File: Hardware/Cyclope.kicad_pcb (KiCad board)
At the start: 2 copper layers, 30 x 100 mm, 75 parts, among them J1 M20-9762042, J2 Motor_2, J3 Motor_1, J4 Front, J5 Front, J8 FTDI, M1 FS5113R, M2 FS5113R, Q1 DMG3414U, Q2 DMG2301L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

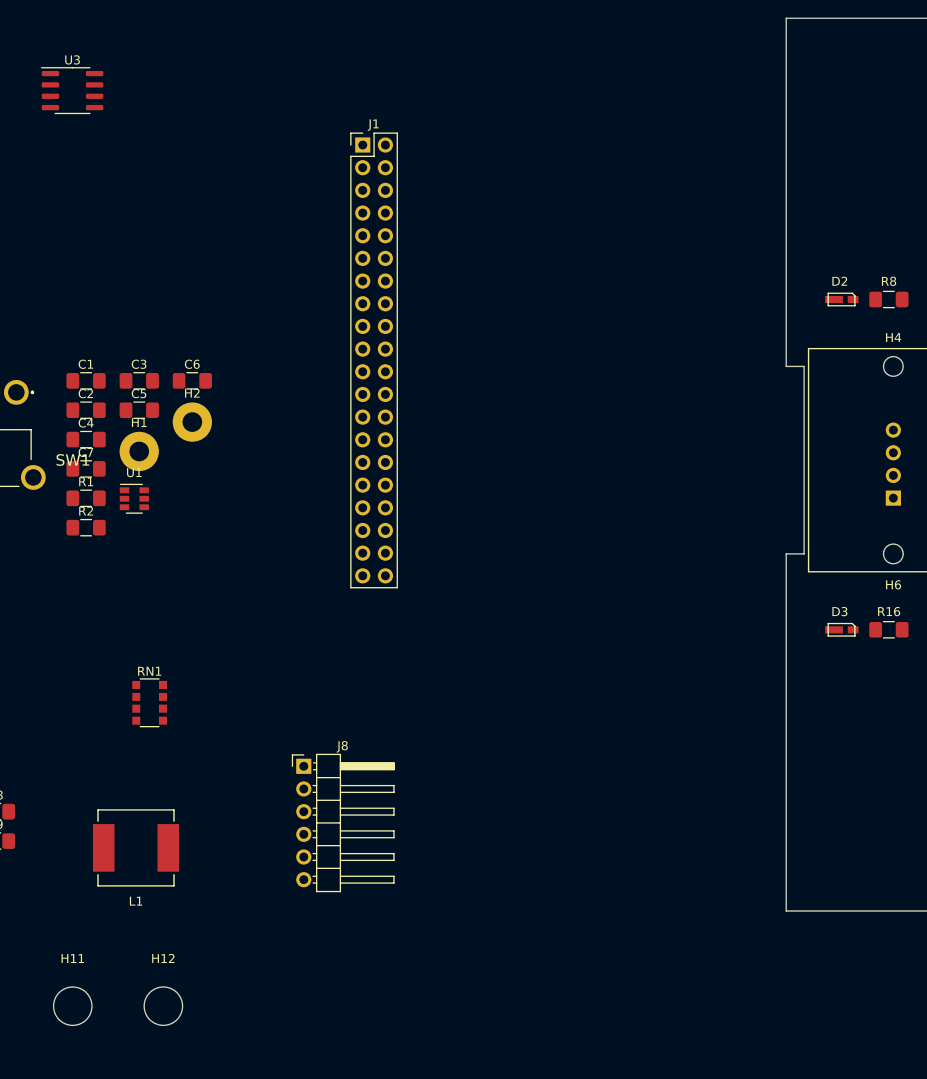
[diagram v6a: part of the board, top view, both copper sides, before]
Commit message: [Hardware] Changed front board mounting holes footprint to match angle bracket holes and positionned holes on front board PCB.
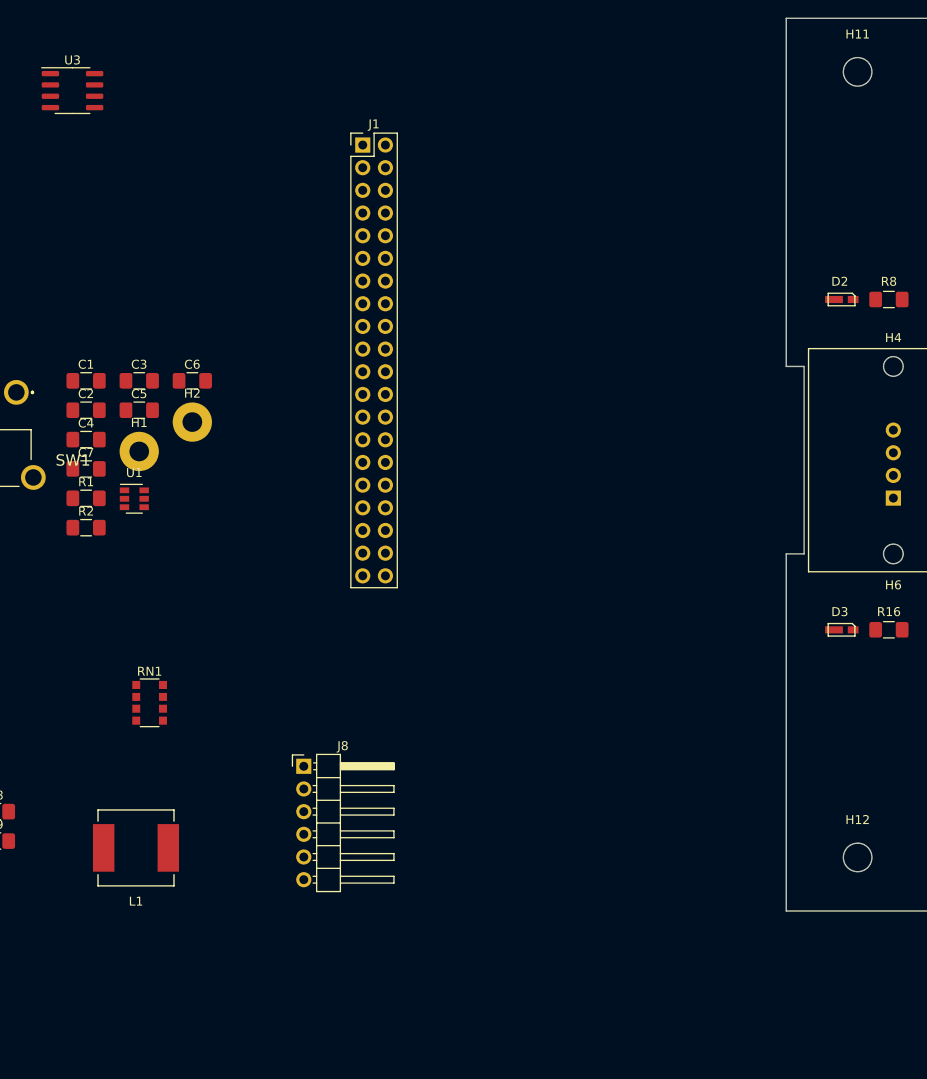
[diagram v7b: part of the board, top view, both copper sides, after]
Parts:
- H11, H12: footprint MountingHole:MountingHole_4.3mm_M4 -> MountingHole:MountingHole_3.2mm_M3
- moved H11 136.7 mm to (218.0, 36.0)
- moved H12 79.5 mm to (218.0, 124.0)
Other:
- board text added: "Use 8mm instead of 10mm to get some margin."
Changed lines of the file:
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@@
   (general
     (thickness 1.6)
-    (drawings 22)
+    (drawings 27)
     (tracks 0)
     (zones 0)
@@
     (add_net "Net-(SW1-Pad1)")
   )
+  (module MountingHole:MountingHole_3.2mm_M3 (layer F.Cu)
+    (at 218 124)
+    (descr "Mounting Hole 3.2mm, no annular, M3")
+    (tags "mounting hole 3.2mm no annular m3")
+    (attr virtual)
+    (fp_text reference H12 (at 0 -4.2) (layer F.SilkS)
+      (effects (font (size 1 1) (thickness 0.15)))
+    )
+    (fp_text value Front_Board (at 0 4.2) (layer F.Fab)
+      (effects (font (size 1 1) (thickness 0.15)))
+    )
+    (fp_circle (center 0 0) (end 3.45 0) (layer F.CrtYd) (width 0.05))
+    (fp_circle (center 0 0) (end 3.2 0) (layer Cmts.User) (width 0.15))
+    (fp_text user %R (at 0.3 0) (layer F.Fab)
+      (effects (font (size 1 1) (thickness 0.15)))
+    )
+    (pad 1 np_thru_hole circle (at 0 0) (size 3.2 3.2) (drill 3.2) (layers *.Cu *.Mask))
+  )
+  (module MountingHole:MountingHole_3.2mm_M3 (layer F.Cu)
+    (at 218 36)
+    (descr "Mounting Hole 3.2mm, no annular, M3")
+    (tags "mounting hole 3.2mm no annular m3")
+    (attr virtual)
+    (fp_text reference H11 (at 0 -4.2) (layer F.SilkS)
+      (effects (font (size 1 1) (thickness 0.15)))
+    )
+    (fp_text value Front_Board (at 0 4.2) (layer F.Fab)
+      (effects (font (size 1 1) (thickness 0.15)))
+    )
+    (fp_circle (center 0 0) (end 3.45 0) (layer F.CrtYd) (width 0.05))
+    (fp_circle (center 0 0) (end 3.2 0) (layer Cmts.User) (width 0.15))
+    (fp_text user %R (at 0.3 0) (layer F.Fab)
+      (effects (font (size 1 1) (thickness 0.15)))
+    )
+    (pad 1 np_thru_hole circle (at 0 0) (size 3.2 3.2) (drill 3.2) (layers *.Cu *.Mask))
+  )
   (module Resistor_SMD:R_1206_3216Metric_Pad1.42x1.75mm_HandSolder (layer F.Cu)
     (at 228.5 98.5)
@@
       (rotate (xyz 0 0 0))
     )
-  )
-  (module MountingHole:MountingHole_4.3mm_M4 (layer F.Cu)
-    (at 140.225001 140.665)
-    (descr "Mounting Hole 4.3mm, no annular, M4")
-    (tags "mounting hole 4.3mm no annular m4")
-    (attr virtual)
-    (fp_text reference H12 (at 0 -5.3) (layer F.SilkS)
-      (effects (font (size 1 1) (thickness 0.15)))
-    )
-    (fp_text value Front_Board (at 0 5.3) (layer F.Fab) hide
-      (effects (font (size 1 1) (thickness 0.15)))
-    )
-    (fp_circle (center 0 0) (end 4.55 0) (layer F.CrtYd) (width 0.05))
-    (fp_circle (center 0 0) (end 4.3 0) (layer Cmts.User) (width 0.15))
-    (fp_text user %R (at 0.3 0) (layer F.Fab)
-      (effects (font (size 1 1) (thickness 0.15)))
-    )
-    (pad 1 np_thru_hole circle (at 0 0) (size 4.3 4.3) (drill 4.3) (layers *.Cu *.Mask))
-  )
-  (module MountingHole:MountingHole_4.3mm_M4 (layer F.Cu)
-    (at 130.075001 140.665)
-    (descr "Mounting Hole 4.3mm, no annular, M4")
-    (tags "mounting hole 4.3mm no annular m4")
-    (attr virtual)
-    (fp_text reference H11 (at 0 -5.3) (layer F.SilkS)
-      (effects (font (size 1 1) (thickness 0.15)))
-    )
-    (fp_text value Front_Board (at 0 5.3) (layer F.Fab) hide
-      (effects (font (size 1 1) (thickness 0.15)))
-    )
-    (fp_circle (center 0 0) (end 4.55 0) (layer F.CrtYd) (width 0.05))
-    (fp_circle (center 0 0) (end 4.3 0) (layer Cmts.User) (width 0.15))
-    (fp_text user %R (at 0.3 0) (layer F.Fab)
-      (effects (font (size 1 1) (thickness 0.15)))
-    )
-    (pad 1 np_thru_hole circle (at 0 0) (size 4.3 4.3) (drill 4.3) (layers *.Cu *.Mask))
   )
   (module 158301250:158301250 (layer F.Cu)
@@
     )
   )
+  (dimension 8 (width 0.15) (layer Dwgs.User)
+    (gr_text "8,000 mm" (at 214 134.3) (layer Dwgs.User)
+      (effects (font (size 1 1) (thickness 0.15)))
+    )
+    (feature1 (pts (xy 218 130) (xy 218 133.586421)))
+    (feature2 (pts (xy 210 130) (xy 210 133.586421)))
+    (crossbar (pts (xy 210 133) (xy 218 133)))
+    (arrow1a (pts (xy 218 133) (xy 216.873496 133.586421)))
+    (arrow1b (pts (xy 218 133) (xy 216.873496 132.413579)))
+    (arrow2a (pts (xy 210 133) (xy 211.126504 133.586421)))
+    (arrow2b (pts (xy 210 133) (xy 211.126504 132.413579)))
+  )
+  (dimension 12 (width 0.15) (layer Dwgs.User)
+    (gr_text "12,000 mm" (at 205.7 124 90) (layer Dwgs.User)
+      (effects (font (size 1 1) (thickness 0.15)))
+    )
+    (feature1 (pts (xy 210 118) (xy 206.413579 118)))
+    (feature2 (pts (xy 210 130) (xy 206.413579 130)))
+    (crossbar (pts (xy 207 130) (xy 207 118)))
+    (arrow1a (pts (xy 207 118) (xy 207.586421 119.126504)))
+    (arrow1b (pts (xy 207 118) (xy 206.413579 119.126504)))
+    (arrow2a (pts (xy 207 130) (xy 207.586421 128.873496)))
+    (arrow2b (pts (xy 207 130) (xy 206.413579 128.873496)))
+  )
+  (gr_text "Use 8mm instead of 10mm\nto get some margin." (at 224 21) (layer Dwgs.User)
+    (effects (font (size 1 1) (thickness 0.15)))
+  )
+  (dimension 8 (width 0.15) (layer Dwgs.User)
+    (gr_text "8,000 mm" (at 214 25.7) (layer Dwgs.User)
+      (effects (font (size 1 1) (thickness 0.15)))
+    )
+    (feature1 (pts (xy 218 30) (xy 218 26.413579)))
+    (feature2 (pts (xy 210 30) (xy 210 26.413579)))
+    (crossbar (pts (xy 210 27) (xy 218 27)))
+    (arrow1a (pts (xy 218 27) (xy 216.873496 27.586421)))
+    (arrow1b (pts (xy 218 27) (xy 216.873496 26.413579)))
+    (arrow2a (pts (xy 210 27) (xy 211.126504 27.586421)))
+    (arrow2b (pts (xy 210 27) (xy 211.126504 26.413579)))
+  )
+  (dimension 12 (width 0.15) (layer Dwgs.User)
+    (gr_text "12,000 mm" (at 205.7 36 270) (layer Dwgs.User)
+      (effects (font (size 1 1) (thickness 0.15)))
+    )
+    (feature1 (pts (xy 210 42) (xy 206.413579 42)))
+    (feature2 (pts (xy 210 30) (xy 206.413579 30)))
+    (crossbar (pts (xy 207 30) (xy 207 42)))
+    (arrow1a (pts (xy 207 42) (xy 206.413579 40.873496)))
+    (arrow1b (pts (xy 207 42) (xy 207.586421 40.873496)))
+    (arrow2a (pts (xy 207 30) (xy 206.413579 31.126504)))
+    (arrow2b (pts (xy 207 30) (xy 207.586421 31.126504)))
+  )
   (gr_line (start 210 90) (end 210 130) (layer Edge.Cuts) (width 0.1))

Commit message: [Hardware] Rotated front board PCB to make edition easier.
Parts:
- moved C1 187.6 mm to (-53.4, 39.6)
- moved C10 187.6 mm to (-71.0, 89.7)
- moved C11 187.6 mm to (-85.8, 96.2)
- moved C12 187.6 mm to (-81.4, 90.8)
- moved C13 187.6 mm to (-84.2, 87.9)
- moved C14 187.6 mm to (-87.0, 17.3)
- moved C15 187.6 mm to (-75.7, 14.6)
- moved C16 187.6 mm to (-66.4, 4.86)
- moved C17 187.6 mm to (-66.4, 8.15)
- moved C18 187.6 mm to (-125.1, 67.0)
- moved C19 187.6 mm to (-119.1, 67.0)
- moved C2 187.6 mm to (-53.4, 42.9)
- moved C3 187.6 mm to (-47.5, 39.6)
- moved C4 187.6 mm to (-53.4, 46.2)
- moved C5 187.6 mm to (-47.5, 42.9)
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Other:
- board size 30 x 100 mm -> 100 x 30 mm
